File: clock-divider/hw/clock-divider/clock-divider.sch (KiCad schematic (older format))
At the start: 47 parts

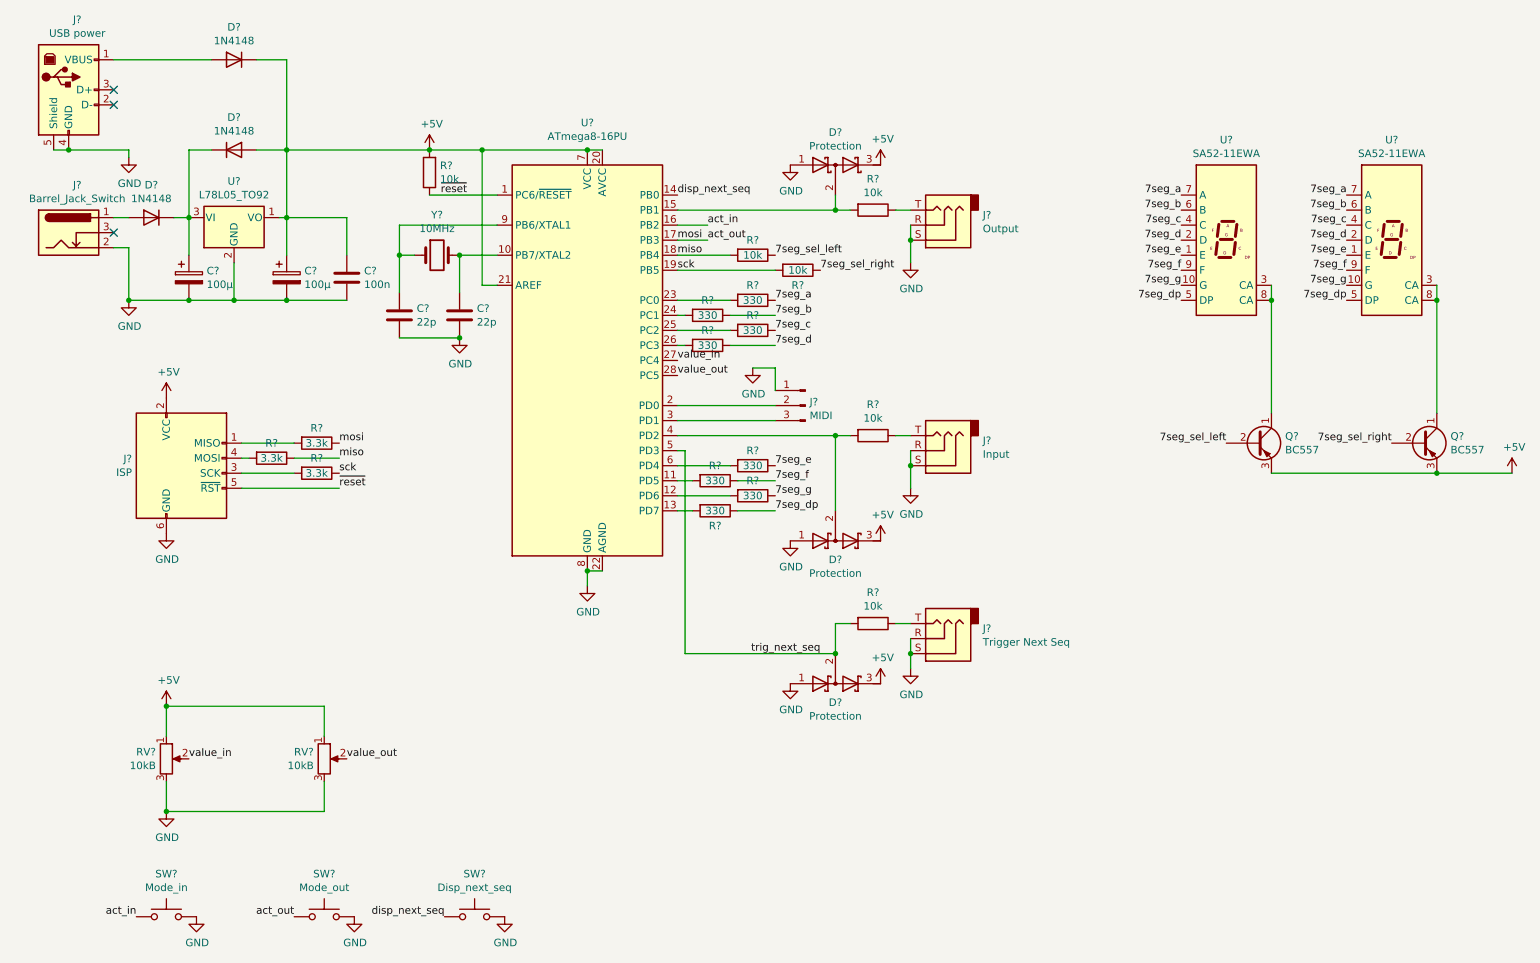
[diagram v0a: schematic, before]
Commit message: clock-divier: hw: annotate schem and add footprints
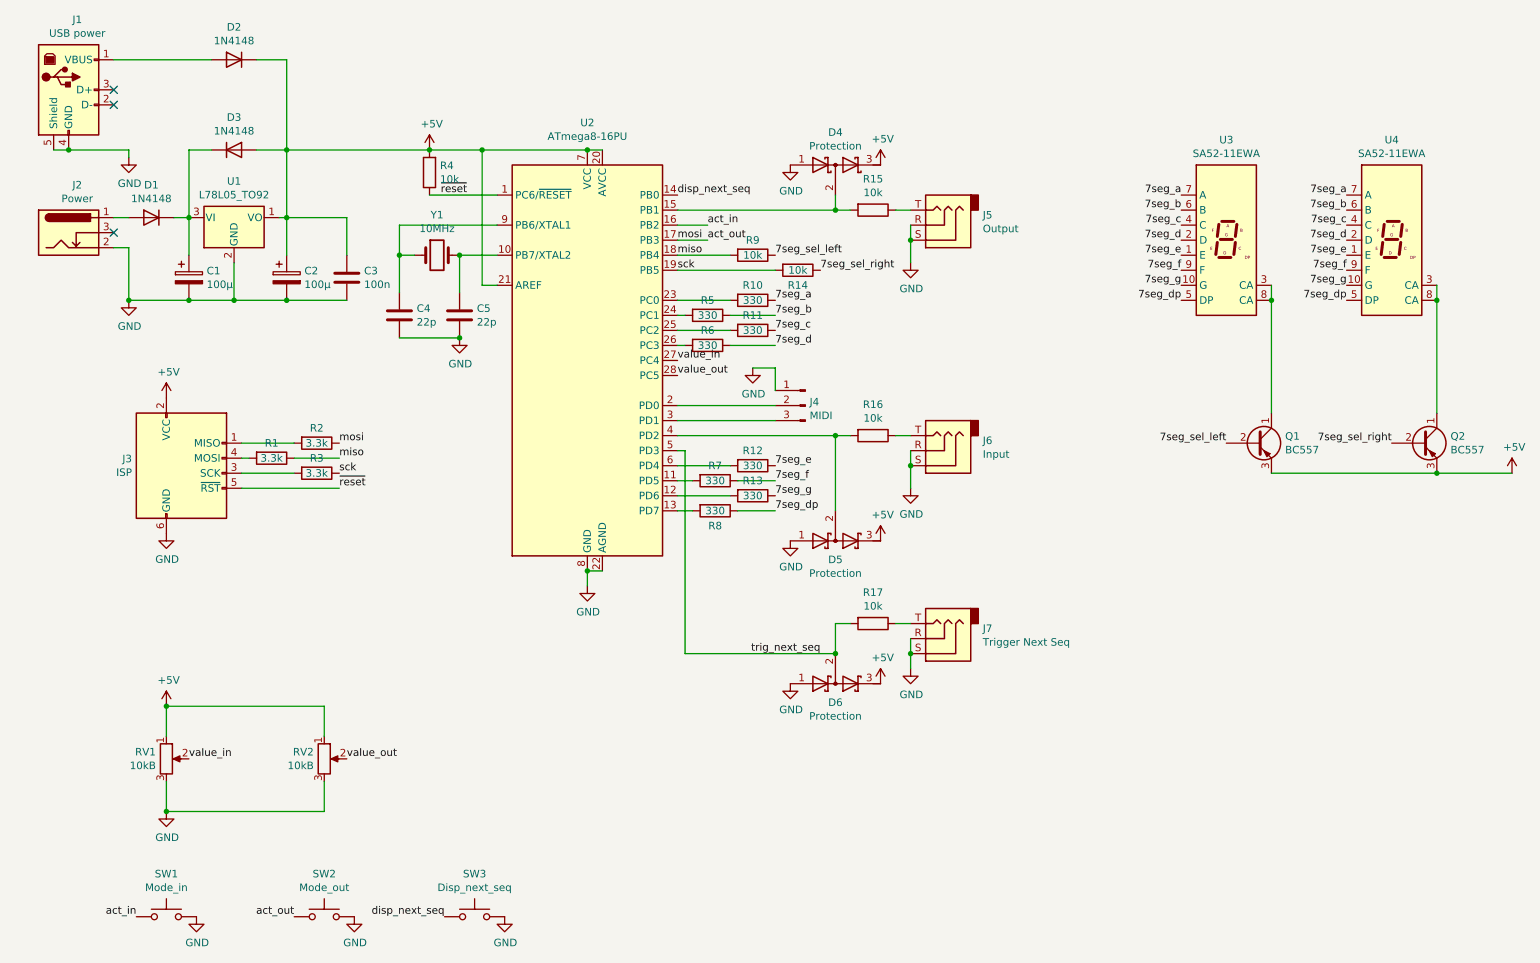
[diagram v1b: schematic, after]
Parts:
- J2: renamed from J?; value Barrel_Jack_Switch -> Power
- gave numbers to parts that had none: 46

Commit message: clock-divider: assign almost all footprints
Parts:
- C1, C2: footprint (none) -> Capacitor_THT:CP_Radial_D6.3mm_P2.50mm
- C3: footprint (none) -> Capacitor_THT:C_Disc_D4.7mm_W2.5mm_P5.00mm
- C4, C5: footprint (none) -> Capacitor_THT:C_Disc_D3.0mm_W2.0mm_P2.50mm
- D1, D2, D3: footprint (none) -> Diode_THT:D_A-405_P7.62mm_Horizontal
- D4, D5, D6: footprint (none) -> Package_TO_SOT_SMD:SOT-23_Handsoldering
- J1: footprint (none) -> Connector_USB:USB_B_Lumberg_2411_02_Horizontal
- J2: footprint (none) -> Connector_BarrelJack:BarrelJack_Horizontal
- J3: footprint (none) -> Connector_IDC:IDC-Header_2x03_P2.54mm_Vertical
- J4: footprint (none) -> Connector_PinHeader_2.54mm:PinHeader_1x03_P2.54mm_Vertical
- R1, R10, R11, R12, R13, R14, R15, R16, R17, R2, R3, R4, R5, R6, R7, R8, R9: footprint (none) -> Resistor_THT:R_Axial_DIN0207_L6.3mm_D2.5mm_P10.16mm_Horizontal
- RV1, RV2: footprint (none) -> Potentiometer_THT:Potentiometer_Alpha_RD901F-40-00D_Single_Vertical_CircularHoles
- SW1, SW2, SW3: footprint (none) -> Button_Switch_THT:SW_PUSH_6mm_H8.5mm
- U3, U4: footprint Display_7Segment:Sx52-1xxxxx -> special-parts:Sx52-1xxxxx
- Y1: footprint (none) -> Crystal:Crystal_HC49-4H_Vertical
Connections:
- net GND: no longer J5.R, J5.S

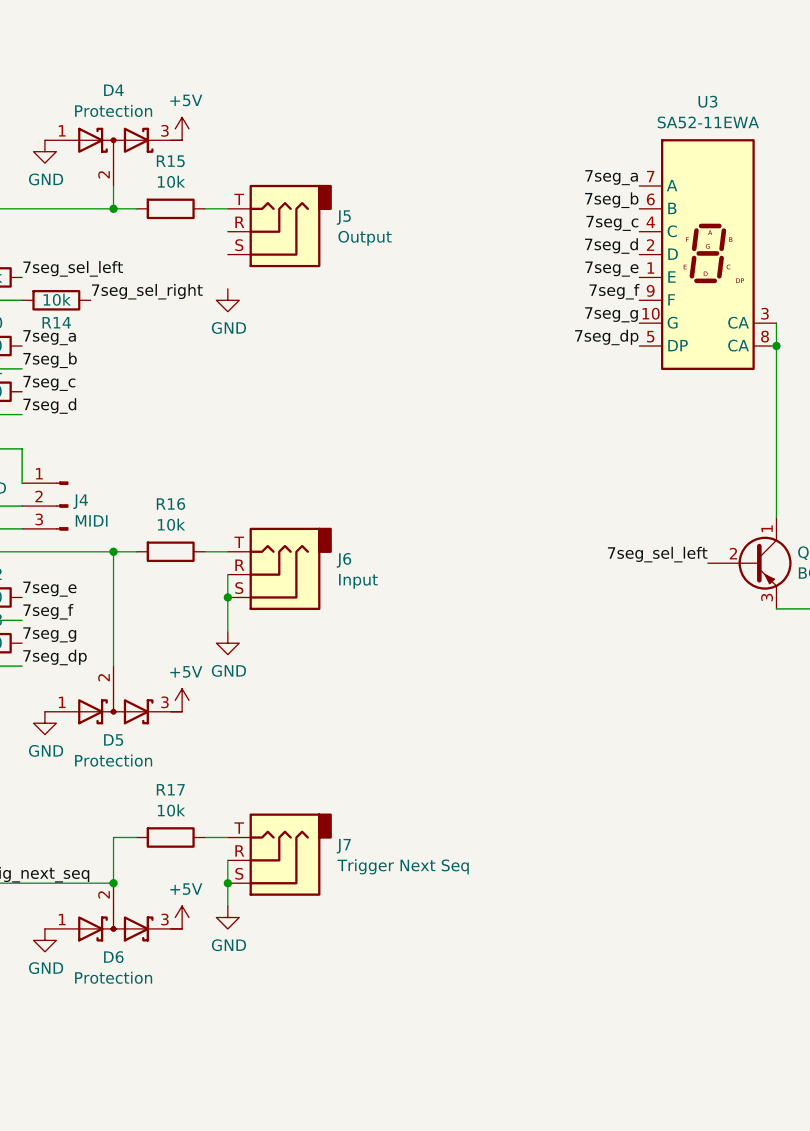
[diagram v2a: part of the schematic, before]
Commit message: clock-divider: replace jacks with PO-style jacks
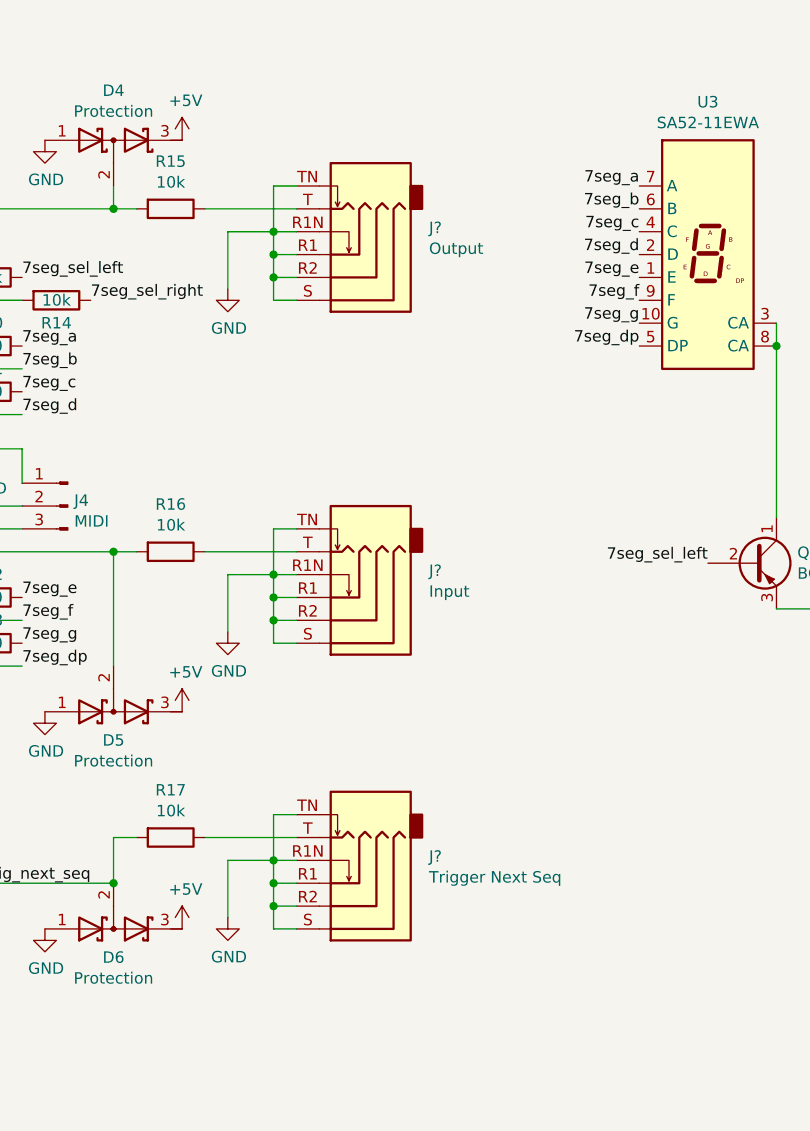
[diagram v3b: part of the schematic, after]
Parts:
- removed J5: Output, symbol Connector:AudioJack3
- removed J6: Input, symbol Connector:AudioJack3
- removed J7: Trigger Next Seq, symbol Connector:AudioJack3
- added J?: Output, symbol Connector:AudioJack4_SwitchTR1
- added J?: Input, symbol Connector:AudioJack4_SwitchTR1
- added J?: Trigger Next Seq, symbol Connector:AudioJack4_SwitchTR1
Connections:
- net GND: now also J?.R1, J?.R1, J?.R1, J?.R1N, J?.R1N, J?.R1N, J?.R2, J?.R2, J?.R2, J?.S, J?.S, J?.S, J?.TN, J?.TN, J?.TN
- net at R16.1: now also J?.T
- net at R15.1: now also J?.T
- net at R17.1: now also J?.T
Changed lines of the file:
@@
-$EndComp
-$Comp
-L Connector:AudioJack3 J6
-U 1 1 60561A84
-P 6650 3500
-F 0 "J6" H 6370 3433 50  0000 R CNN
-F 1 "Input" H 6370 3524 50  0000 R CNN
-F 2 "" H 6650 3500 50  0001 C CNN
-F 3 "~" H 6650 3500 50  0001 C CNN
-	1    6650 3500
-	-1   0    0    1
-$EndComp
-$Comp
-L Connector:AudioJack3 J5
-U 1 1 6056207B
-P 6650 2000
-F 0 "J5" H 6370 1933 50  0000 R CNN
-F 1 "Output" H 6370 2024 50  0000 R CNN
-F 2 "" H 6650 2000 50  0001 C CNN
-F 3 "~" H 6650 2000 50  0001 C CNN
-	1    6650 2000
-	-1   0    0    1
 $EndComp
 $Comp
@@
 	0    1    1    0
 $EndComp
-Wire Wire Line
-	6350 1900 6450 1900
 $Comp
 L power:GND #PWR020
@@
 Wire Wire Line
 	6050 3400 5950 3400
-Wire Wire Line
-	6450 3400 6350 3400
-$Comp
-L power:GND #PWR021
-U 1 1 605DA853
-P 6450 3750
-F 0 "#PWR021" H 6450 3500 50  0001 C CNN
-F 1 "GND" H 6455 3577 50  0000 C CNN
-F 2 "" H 6450 3750 50  0001 C CNN
-F 3 "" H 6450 3750 50  0001 C CNN
-	1    6450 3750
-	1    0    0    -1
-$EndComp
-Wire Wire Line
-	6450 3750 6450 3600
-Connection ~ 6450 3600
-Wire Wire Line
-	6450 3600 6450 3500
 Wire Wire Line
 	1950 2250 1950 2500
@@
 Text Label 5550 2200 0    50   ~ 0
 7seg_sel_left
-$Comp
-L Connector:AudioJack3 J7
-U 1 1 6074DC5A
-P 6650 4750
-F 0 "J7" H 6370 4683 50  0000 R CNN
-F 1 "Trigger Next Seq" H 6370 4774 50  0000 R CNN
-F 2 "" H 6650 4750 50  0001 C CNN
-F 3 "~" H 6650 4750 50  0001 C CNN
-	1    6650 4750
-	-1   0    0    1
-$EndComp
-$Comp
-L power:GND #PWR022
-U 1 1 607503C1
-P 6450 4950
-F 0 "#PWR022" H 6450 4700 50  0001 C CNN
-F 1 "GND" H 6455 4777 50  0000 C CNN
-F 2 "" H 6450 4950 50  0001 C CNN
-F 3 "" H 6450 4950 50  0001 C CNN
-	1    6450 4950
-	1    0    0    -1
-$EndComp
-Wire Wire Line
-	6450 4750 6450 4850
-Connection ~ 6450 4850
-Wire Wire Line
-	6450 4850 6450 4950
 Text Label 5850 4850 2    50   ~ 0
 trig_next_seq
@@
 	5950 4850 5950 4650
 Wire Wire Line
-	6350 4650 6450 4650
-Wire Wire Line
 	6050 4650 5950 4650
 Wire Wire Line
@@
 Wire Wire Line
 	2000 3750 2650 3750
+Wire Wire Line
+	6450 2000 6450 2250
+Wire Wire Line
+	6750 1800 6650 1800
+Wire Wire Line
+	6650 1800 6650 2000
+Wire Wire Line
+	6650 2000 6750 2000
+Wire Wire Line
+	6350 1900 6750 1900
+Wire Wire Line
+	6450 2000 6650 2000
+Connection ~ 6650 2000
+Wire Wire Line
+	6650 2000 6650 2100
+Wire Wire Line
+	6750 2100 6650 2100
+Connection ~ 6650 2100
+Wire Wire Line
+	6650 2100 6650 2200
+Wire Wire Line
+	6650 2200 6750 2200
+Wire Wire Line
+	6750 3300 6650 3300
+Wire Wire Line
+	6650 3300 6650 3500
+Wire Wire Line
+	6650 3500 6750 3500
+Wire Wire Line
+	6350 3400 6750 3400
+Wire Wire Line
+	6450 3500 6650 3500
+Connection ~ 6650 3500
+Wire Wire Line
+	6650 3500 6650 3600
+Wire Wire Line
+	6750 3600 6650 3600
+Connection ~ 6650 3600
+Wire Wire Line
+	6650 3600 6650 3700
+Wire Wire Line
+	6650 3700 6750 3700
+$Comp
+L power:GND #PWR021
+U 1 1 60C16BDF
+P 6450 3750
+F 0 "#PWR021" H 6450 3500 50  0001 C CNN
+F 1 "GND" H 6455 3577 50  0000 C CNN
+F 2 "" H 6450 3750 50  0001 C CNN
+F 3 "" H 6450 3750 50  0001 C CNN
+	1    6450 3750
+	1    0    0    -1
+$EndComp
+Wire Wire Line
+	6450 3500 6450 3750
+Wire Wire Line
+	6750 4550 6650 4550
+Wire Wire Line
+	6650 4550 6650 4750
+Wire Wire Line
+	6650 4750 6750 4750
+Wire Wire Line
+	6350 4650 6750 4650
+Wire Wire Line
+	6450 4750 6650 4750
+Connection ~ 6650 4750
+Wire Wire Line
+	6650 4750 6650 4850
+Wire Wire Line
+	6750 4850 6650 4850
+Connection ~ 6650 4850
+Wire Wire Line
+	6650 4850 6650 4950
+Wire Wire Line
+	6650 4950 6750 4950
+$Comp
+L power:GND #PWR022
+U 1 1 60C30F65
+P 6450 5000
+F 0 "#PWR022" H 6450 4750 50  0001 C CNN
+F 1 "GND" H 6455 4827 50  0000 C CNN
+F 2 "" H 6450 5000 50  0001 C CNN
+F 3 "" H 6450 5000 50  0001 C CNN
+	1    6450 5000
+	1    0    0    -1
+$EndComp
+Wire Wire Line
+	6450 4750 6450 5000
+Connection ~ 6650 4950
+Wire Wire Line
+	6650 4950 6650 5050
+Wire Wire Line
+	6650 5050 6750 5050
+Connection ~ 6650 3700
+Wire Wire Line
+	6650 3700 6650 3800
+Wire Wire Line
+	6650 3800 6750 3800
+Connection ~ 6650 2200
+Wire Wire Line
+	6650 2200 6650 2300
+Wire Wire Line
+	6650 2300 6750 2300
+$Comp
+L Connector:AudioJack4_SwitchTR1 J?
+U 1 1 60CA922E
+P 6950 2100
+F 0 "J?" H 6570 1983 50  0000 R CNN
+F 1 "Output" H 6570 2074 50  0000 R CNN
+F 2 "" H 6900 2100 50  0001 C CNN
+F 3 "~" H 6900 2100 50  0001 C CNN
+	1    6950 2100
+	-1   0    0    1
+$EndComp
+$Comp
+L Connector:AudioJack4_SwitchTR1 J?
+U 1 1 60CBA4F6
+P 6950 3600
+F 0 "J?" H 6570 3483 50  0000 R CNN
+F 1 "Input" H 6570 3574 50  0000 R CNN
+F 2 "" H 6900 3600 50  0001 C CNN
+F 3 "~" H 6900 3600 50  0001 C CNN
+	1    6950 3600
+	-1   0    0    1
+$EndComp
+$Comp
+L Connector:AudioJack4_SwitchTR1 J?
+U 1 1 60CC0409
+P 6950 4850
+F 0 "J?" H 6570 4733 50  0000 R CNN
+F 1 "Trigger Next Seq" H 6570 4824 50  0000 R CNN
+F 2 "" H 6900 4850 50  0001 C CNN
+F 3 "~" H 6900 4850 50  0001 C CNN
+	1    6950 4850
+	-1   0    0    1
+$EndComp
 $EndSCHEMATC

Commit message: clock-divider: annotate new jacks
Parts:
- gave numbers to parts that had none: 3
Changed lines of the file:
@@
 	6650 2300 6750 2300
 $Comp
-L Connector:AudioJack4_SwitchTR1 J?
+L Connector:AudioJack4_SwitchTR1 J5
 U 1 1 60CA922E
 P 6950 2100
-F 0 "J?" H 6570 1983 50  0000 R CNN
+F 0 "J5" H 6570 1983 50  0000 R CNN
 F 1 "Output" H 6570 2074 50  0000 R CNN
 F 2 "" H 6900 2100 50  0001 C CNN
@@
 $EndComp
 $Comp
-L Connector:AudioJack4_SwitchTR1 J?
+L Connector:AudioJack4_SwitchTR1 J6
 U 1 1 60CBA4F6
 P 6950 3600
-F 0 "J?" H 6570 3483 50  0000 R CNN
+F 0 "J6" H 6570 3483 50  0000 R CNN
 F 1 "Input" H 6570 3574 50  0000 R CNN
 F 2 "" H 6900 3600 50  0001 C CNN
@@
 $EndComp
 $Comp
-L Connector:AudioJack4_SwitchTR1 J?
+L Connector:AudioJack4_SwitchTR1 J7
 U 1 1 60CC0409
 P 6950 4850
-F 0 "J?" H 6570 4733 50  0000 R CNN
+F 0 "J7" H 6570 4733 50  0000 R CNN
 F 1 "Trigger Next Seq" H 6570 4824 50  0000 R CNN
 F 2 "" H 6900 4850 50  0001 C CNN

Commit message: clock-divider: update footprints in schematic
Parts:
- J5, J6, J7: footprint (none) -> special-parts:Jack_3.5mm_CUI_SJ-43516-SMT_Horizontal
- Q1, Q2, U1: footprint Package_TO_SOT_THT:TO-92_Inline -> Package_TO_SOT_THT:TO-92_Inline_Wide
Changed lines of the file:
@@
 F 0 "U1" H 1950 2192 50  0000 C CNN
 F 1 "L78L05_TO92" H 1950 2101 50  0000 C CNN
-F 2 "Package_TO_SOT_THT:TO-92_Inline" H 1950 2175 50  0001 C CIN
+F 2 "Package_TO_SOT_THT:TO-92_Inline_Wide" H 1950 2175 50  0001 C CIN
 F 3 "http://www.st.com/content/ccc/resource/technical/document/datasheet/15/55/e5/aa/23/5b/43/fd/CD00000446.pdf/files/CD00000446.pdf/jcr:content/translations/en.CD00000446.pdf" H 1950 1900 50  0001 C CNN
 	1    1950 1950
@@
 F 0 "Q1" H 8941 3496 50  0000 L CNN
 F 1 "BC557" H 8941 3405 50  0000 L CNN
-F 2 "Package_TO_SOT_THT:TO-92_Inline" H 8950 3375 50  0001 L CIN
+F 2 "Package_TO_SOT_THT:TO-92_Inline_Wide" H 8950 3375 50  0001 L CIN
 F 3 "https://www.onsemi.com/pub/Collateral/BC556BTA-D.pdf" H 8750 3450 50  0001 L CNN
 	1    8750 3450
@@
 F 0 "Q2" H 10041 3496 50  0000 L CNN
 F 1 "BC557" H 10041 3405 50  0000 L CNN
-F 2 "Package_TO_SOT_THT:TO-92_Inline" H 10050 3375 50  0001 L CIN
+F 2 "Package_TO_SOT_THT:TO-92_Inline_Wide" H 10050 3375 50  0001 L CIN
 F 3 "https://www.onsemi.com/pub/Collateral/BC556BTA-D.pdf" H 9850 3450 50  0001 L CNN
 	1    9850 3450
@@
 F 0 "J5" H 6570 1983 50  0000 R CNN
 F 1 "Output" H 6570 2074 50  0000 R CNN
-F 2 "" H 6900 2100 50  0001 C CNN
+F 2 "special-parts:Jack_3.5mm_CUI_SJ-43516-SMT_Horizontal" H 6900 2100 50  0001 C CNN
 F 3 "~" H 6900 2100 50  0001 C CNN
 	1    6950 2100
@@
 F 0 "J6" H 6570 3483 50  0000 R CNN
 F 1 "Input" H 6570 3574 50  0000 R CNN
-F 2 "" H 6900 3600 50  0001 C CNN
+F 2 "special-parts:Jack_3.5mm_CUI_SJ-43516-SMT_Horizontal" H 6900 3600 50  0001 C CNN
 F 3 "~" H 6900 3600 50  0001 C CNN
 	1    6950 3600
@@
 F 0 "J7" H 6570 4733 50  0000 R CNN
 F 1 "Trigger Next Seq" H 6570 4824 50  0000 R CNN
-F 2 "" H 6900 4850 50  0001 C CNN
+F 2 "special-parts:Jack_3.5mm_CUI_SJ-43516-SMT_Horizontal" H 6900 4850 50  0001 C CNN
 F 3 "~" H 6900 4850 50  0001 C CNN
 	1    6950 4850
